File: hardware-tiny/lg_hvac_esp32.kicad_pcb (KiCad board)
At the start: 4 copper layers, 29 x 50.3 mm, 16 parts, among them J1 JST_XH_S3B-XH-A-1_01x03, J2 Conn_01x19_Female_1_to_19, J3 Conn_01x19_Female_20_to_38, U1 TPS82130, U2 TJA1027

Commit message: fixed bom and updated kicad project to kicad7 #17
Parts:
- U1: footprint TPS82130:CONV_TPS82140SILR -> Package_LGA:Texas_SIL0008D_MicroSiP-8-1EP_2.8x3mm_P0.65mm_EP1.1x1.9mm_ThermalVias

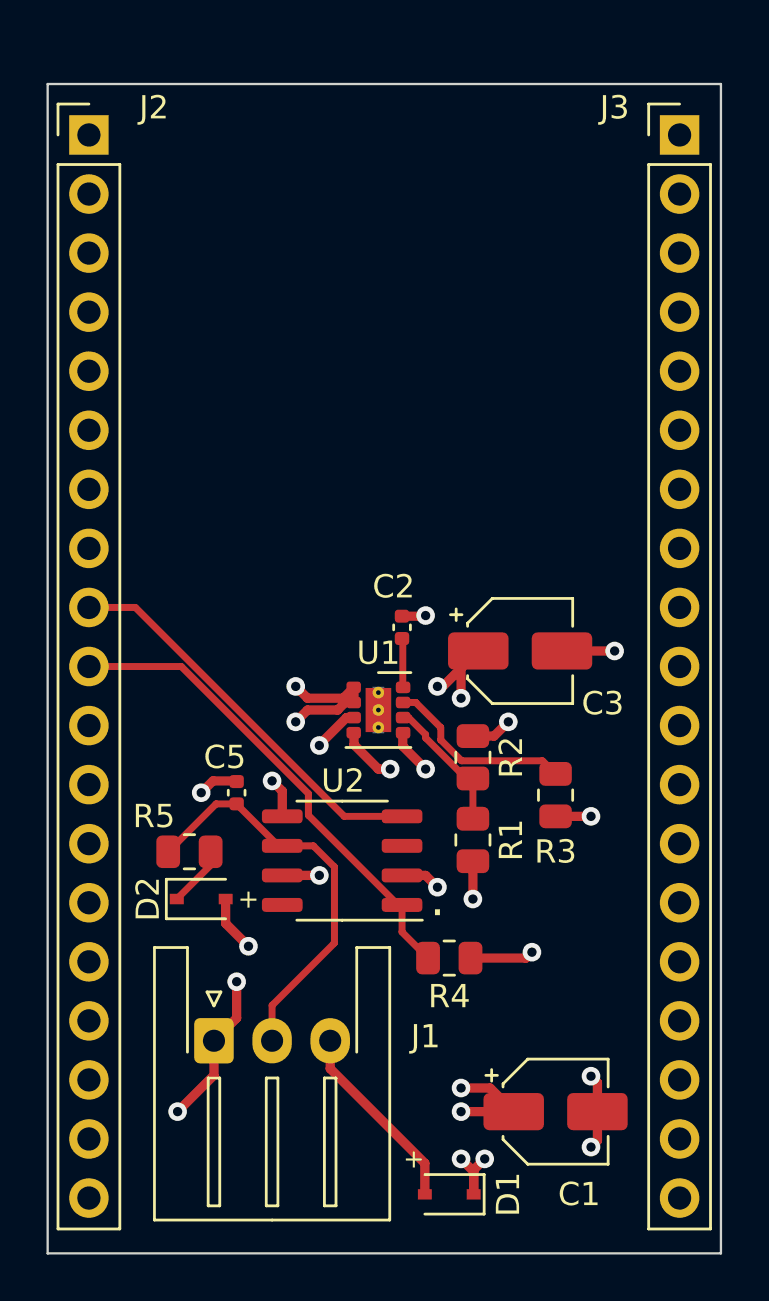
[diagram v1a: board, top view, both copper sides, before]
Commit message: fixes in schematic & bom, removed C3
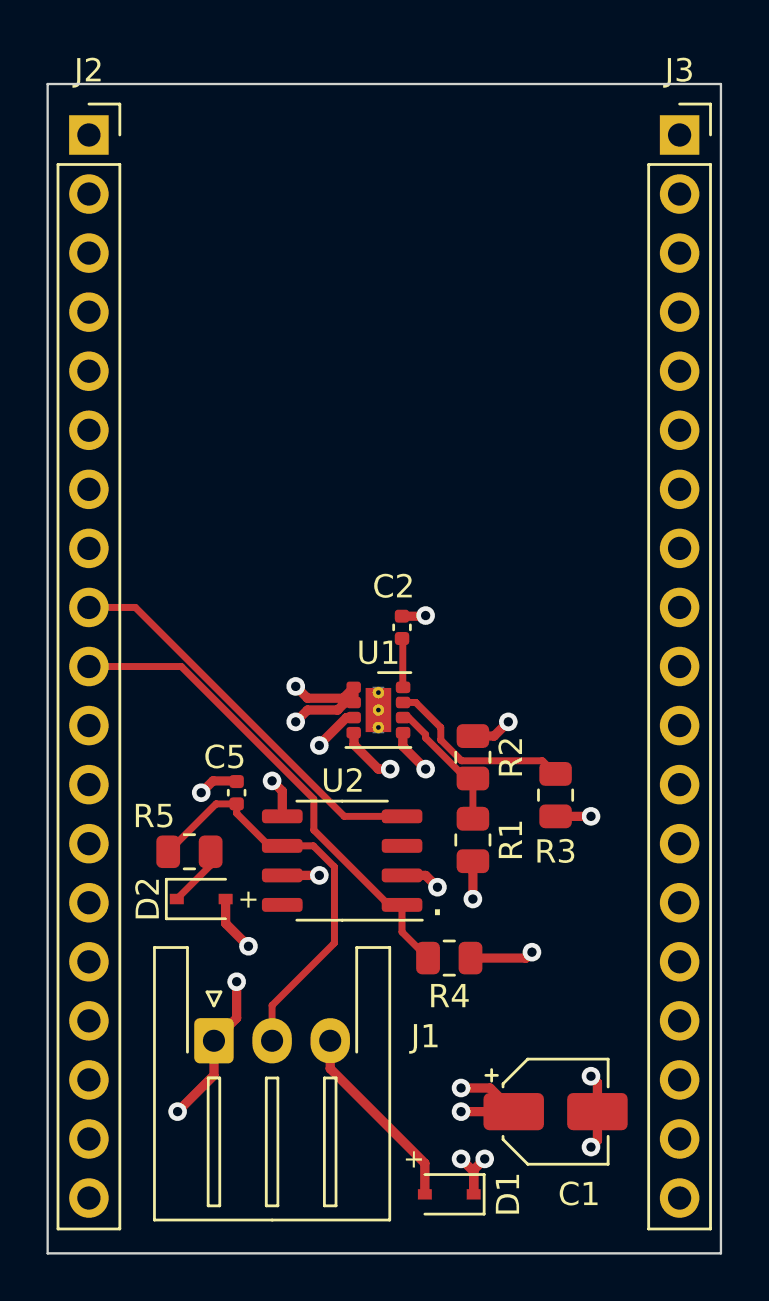
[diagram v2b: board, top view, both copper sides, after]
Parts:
- removed C3: 22uF, Capacitor_SMD:CP_Elec_4x5.8
- J2, J3: footprint Connector_PinHeader_2.54mm:PinHeader_1x19_P2.54mm_Vertical -> Connector_PinSocket_2.54mm:PinSocket_1x19_P2.54mm_Vertical
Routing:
- net +3V3: track 16.8 -> 12.1 mm, vias 8 -> 6
- net GND: track 20.4 -> 18.2 mm, vias 10 -> 9
